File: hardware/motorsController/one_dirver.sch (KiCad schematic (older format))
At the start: 9 parts, among them U1 VNH5019A-E

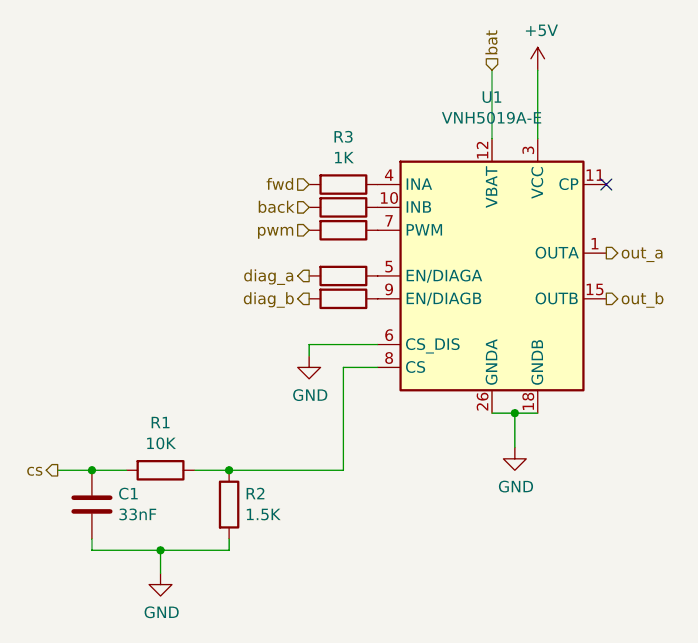
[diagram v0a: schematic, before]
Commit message: layout and connect power for a pair of drivers
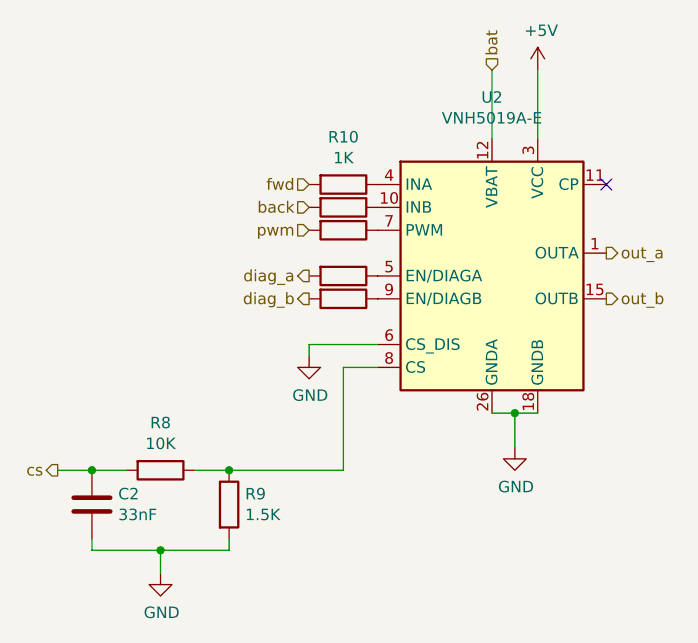
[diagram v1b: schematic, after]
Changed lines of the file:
@@
 $Descr A4 11693 8268
 encoding utf-8
-Sheet 2 5
+Sheet 3 5
 Title ""
 Date ""
@@
 AR Path="/5F8B7961/5F75DD74" Ref="U3"  Part="1"
 AR Path="/5F8B7981/5F75DD74" Ref="U4"  Part="1"
-F 0 "U1" H 3150 3531 50  0000 C CNN
+F 0 "U2" H 3150 3531 50  0000 C CNN
 F 1 "VNH5019A-E" H 3150 3440 50  0000 C CNN
 F 2 "Package_SO:ST_MultiPowerSO-30" H 4050 2200 50  0001 C CNN
@@
 AR Path="/5F8B7961/5F764A13" Ref="R17"  Part="1"
 AR Path="/5F8B7981/5F764A13" Ref="R24"  Part="1"
-F 0 "R3" V 2293 2350 50  0000 C CNN
+F 0 "R10" V 2293 2350 50  0000 C CNN
 F 1 "1K" V 2384 2350 50  0000 C CNN
 F 2 "Resistor_SMD:R_0805_2012Metric" V 2430 2350 50  0001 C CNN
@@
 AR Path="/5F8B7961/5F765406" Ref="R18"  Part="1"
 AR Path="/5F8B7981/5F765406" Ref="R25"  Part="1"
-F 0 "R4" V 2293 2450 50  0001 C CNN
+F 0 "R11" V 2293 2450 50  0001 C CNN
 F 1 "1K" V 2384 2450 50  0001 C CNN
 F 2 "Resistor_SMD:R_0805_2012Metric" V 2430 2450 50  0001 C CNN
@@
 AR Path="/5F8B7961/5F7658F2" Ref="R19"  Part="1"
 AR Path="/5F8B7981/5F7658F2" Ref="R26"  Part="1"
-F 0 "R5" V 2293 2550 50  0001 C CNN
+F 0 "R12" V 2293 2550 50  0001 C CNN
 F 1 "1K" V 2384 2550 50  0001 C CNN
 F 2 "Resistor_SMD:R_0805_2012Metric" V 2430 2550 50  0001 C CNN
@@
 AR Path="/5F8B7961/5F77E0ED" Ref="R20"  Part="1"
 AR Path="/5F8B7981/5F77E0ED" Ref="R27"  Part="1"
-F 0 "R6" V 2293 2750 50  0001 C CNN
+F 0 "R13" V 2293 2750 50  0001 C CNN
 F 1 "1K" V 2384 2750 50  0001 C CNN
 F 2 "Resistor_SMD:R_0805_2012Metric" V 2430 2750 50  0001 C CNN
@@
 AR Path="/5F8B7961/5F781639" Ref="R21"  Part="1"
 AR Path="/5F8B7981/5F781639" Ref="R28"  Part="1"
-F 0 "R7" V 2293 2850 50  0001 C CNN
+F 0 "R14" V 2293 2850 50  0001 C CNN
 F 1 "1K" V 2384 2850 50  0001 C CNN
 F 2 "Resistor_SMD:R_0805_2012Metric" V 2430 2850 50  0001 C CNN
@@
 AR Path="/5F8B7961/5F781B76" Ref="#PWR0112"  Part="1"
 AR Path="/5F8B7981/5F781B76" Ref="#PWR0116"  Part="1"
-F 0 "#PWR0101" H 2350 2850 50  0001 C CNN
+F 0 "#PWR0108" H 2350 2850 50  0001 C CNN
 F 1 "GND" H 2355 2927 50  0000 C CNN
 F 2 "" H 2350 3100 50  0001 C CNN
@@
 AR Path="/5F8B7961/5F782890" Ref="R16"  Part="1"
 AR Path="/5F8B7981/5F782890" Ref="R23"  Part="1"
-F 0 "R2" H 2070 3796 50  0000 L CNN
+F 0 "R9" H 2070 3796 50  0000 L CNN
 F 1 "1.5K" H 2070 3705 50  0000 L CNN
 F 2 "Resistor_SMD:R_0805_2012Metric" V 1930 3750 50  0001 C CNN
@@
 AR Path="/5F8B7961/5F783B44" Ref="#PWR0113"  Part="1"
 AR Path="/5F8B7981/5F783B44" Ref="#PWR0117"  Part="1"
-F 0 "#PWR0102" H 1700 3800 50  0001 C CNN
+F 0 "#PWR0109" H 1700 3800 50  0001 C CNN
 F 1 "GND" H 1705 3877 50  0000 C CNN
 F 2 "" H 1700 4050 50  0001 C CNN
@@
 AR Path="/5F8B7961/5F7841BA" Ref="R15"  Part="1"
 AR Path="/5F8B7981/5F7841BA" Ref="R22"  Part="1"
-F 0 "R1" V 1493 3600 50  0000 C CNN
+F 0 "R8" V 1493 3600 50  0000 C CNN
 F 1 "10K" V 1584 3600 50  0000 C CNN
 F 2 "Resistor_SMD:R_0805_2012Metric" V 1630 3600 50  0001 C CNN
@@
 AR Path="/5F8B7961/5F784D90" Ref="C3"  Part="1"
 AR Path="/5F8B7981/5F784D90" Ref="C4"  Part="1"
-F 0 "C1" H 1515 3796 50  0000 L CNN
+F 0 "C2" H 1515 3796 50  0000 L CNN
 F 1 "33nF" H 1515 3705 50  0000 L CNN
 F 2 "Capacitor_SMD:C_1206_3216Metric" H 1438 3600 50  0001 C CNN
@@
 AR Path="/5F8B7961/5F78A1BC" Ref="#PWR0114"  Part="1"
 AR Path="/5F8B7981/5F78A1BC" Ref="#PWR0118"  Part="1"
-F 0 "#PWR0103" H 3350 1700 50  0001 C CNN
+F 0 "#PWR0110" H 3350 1700 50  0001 C CNN
 F 1 "+5V" H 3365 2023 50  0000 C CNN
 F 2 "" H 3350 1850 50  0001 C CNN
@@
 AR Path="/5F8B7961/5F794080" Ref="#PWR0115"  Part="1"
 AR Path="/5F8B7981/5F794080" Ref="#PWR0119"  Part="1"
-F 0 "#PWR0104" H 3250 3250 50  0001 C CNN
+F 0 "#PWR0111" H 3250 3250 50  0001 C CNN
 F 1 "GND" H 3255 3327 50  0000 C CNN
 F 2 "" H 3250 3500 50  0001 C CNN

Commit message: connect left-rear driver to arduino
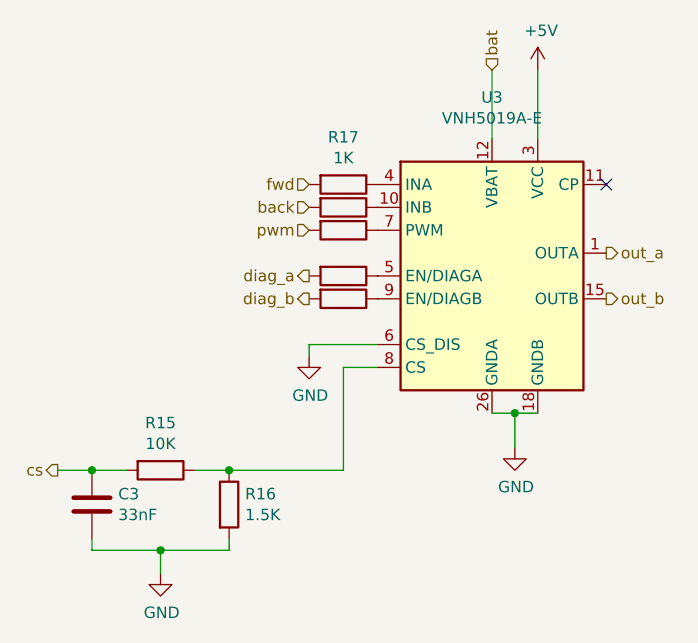
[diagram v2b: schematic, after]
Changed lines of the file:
@@
 $Descr A4 11693 8268
 encoding utf-8
-Sheet 3 5
+Sheet 4 5
 Title ""
 Date ""
@@
 AR Path="/5F8B7961/5F75DD74" Ref="U3"  Part="1"
 AR Path="/5F8B7981/5F75DD74" Ref="U4"  Part="1"
-F 0 "U2" H 3150 3531 50  0000 C CNN
+F 0 "U3" H 3150 3531 50  0000 C CNN
 F 1 "VNH5019A-E" H 3150 3440 50  0000 C CNN
 F 2 "Package_SO:ST_MultiPowerSO-30" H 4050 2200 50  0001 C CNN
@@
 AR Path="/5F8B7961/5F764A13" Ref="R17"  Part="1"
 AR Path="/5F8B7981/5F764A13" Ref="R24"  Part="1"
-F 0 "R10" V 2293 2350 50  0000 C CNN
+F 0 "R17" V 2293 2350 50  0000 C CNN
 F 1 "1K" V 2384 2350 50  0000 C CNN
 F 2 "Resistor_SMD:R_0805_2012Metric" V 2430 2350 50  0001 C CNN
@@
 AR Path="/5F8B7961/5F765406" Ref="R18"  Part="1"
 AR Path="/5F8B7981/5F765406" Ref="R25"  Part="1"
-F 0 "R11" V 2293 2450 50  0001 C CNN
+F 0 "R18" V 2293 2450 50  0001 C CNN
 F 1 "1K" V 2384 2450 50  0001 C CNN
 F 2 "Resistor_SMD:R_0805_2012Metric" V 2430 2450 50  0001 C CNN
@@
 AR Path="/5F8B7961/5F7658F2" Ref="R19"  Part="1"
 AR Path="/5F8B7981/5F7658F2" Ref="R26"  Part="1"
-F 0 "R12" V 2293 2550 50  0001 C CNN
+F 0 "R19" V 2293 2550 50  0001 C CNN
 F 1 "1K" V 2384 2550 50  0001 C CNN
 F 2 "Resistor_SMD:R_0805_2012Metric" V 2430 2550 50  0001 C CNN
@@
 AR Path="/5F8B7961/5F77E0ED" Ref="R20"  Part="1"
 AR Path="/5F8B7981/5F77E0ED" Ref="R27"  Part="1"
-F 0 "R13" V 2293 2750 50  0001 C CNN
+F 0 "R20" V 2293 2750 50  0001 C CNN
 F 1 "1K" V 2384 2750 50  0001 C CNN
 F 2 "Resistor_SMD:R_0805_2012Metric" V 2430 2750 50  0001 C CNN
@@
 AR Path="/5F8B7961/5F781639" Ref="R21"  Part="1"
 AR Path="/5F8B7981/5F781639" Ref="R28"  Part="1"
-F 0 "R14" V 2293 2850 50  0001 C CNN
+F 0 "R21" V 2293 2850 50  0001 C CNN
 F 1 "1K" V 2384 2850 50  0001 C CNN
 F 2 "Resistor_SMD:R_0805_2012Metric" V 2430 2850 50  0001 C CNN
@@
 AR Path="/5F8B7961/5F781B76" Ref="#PWR0112"  Part="1"
 AR Path="/5F8B7981/5F781B76" Ref="#PWR0116"  Part="1"
-F 0 "#PWR0108" H 2350 2850 50  0001 C CNN
+F 0 "#PWR0116" H 2350 2850 50  0001 C CNN
 F 1 "GND" H 2355 2927 50  0000 C CNN
 F 2 "" H 2350 3100 50  0001 C CNN
@@
 AR Path="/5F8B7961/5F782890" Ref="R16"  Part="1"
 AR Path="/5F8B7981/5F782890" Ref="R23"  Part="1"
-F 0 "R9" H 2070 3796 50  0000 L CNN
+F 0 "R16" H 2070 3796 50  0000 L CNN
 F 1 "1.5K" H 2070 3705 50  0000 L CNN
 F 2 "Resistor_SMD:R_0805_2012Metric" V 1930 3750 50  0001 C CNN
@@
 AR Path="/5F8B7961/5F783B44" Ref="#PWR0113"  Part="1"
 AR Path="/5F8B7981/5F783B44" Ref="#PWR0117"  Part="1"
-F 0 "#PWR0109" H 1700 3800 50  0001 C CNN
+F 0 "#PWR0117" H 1700 3800 50  0001 C CNN
 F 1 "GND" H 1705 3877 50  0000 C CNN
 F 2 "" H 1700 4050 50  0001 C CNN
@@
 AR Path="/5F8B7961/5F7841BA" Ref="R15"  Part="1"
 AR Path="/5F8B7981/5F7841BA" Ref="R22"  Part="1"
-F 0 "R8" V 1493 3600 50  0000 C CNN
+F 0 "R15" V 1493 3600 50  0000 C CNN
 F 1 "10K" V 1584 3600 50  0000 C CNN
 F 2 "Resistor_SMD:R_0805_2012Metric" V 1630 3600 50  0001 C CNN
@@
 AR Path="/5F8B7961/5F784D90" Ref="C3"  Part="1"
 AR Path="/5F8B7981/5F784D90" Ref="C4"  Part="1"
-F 0 "C2" H 1515 3796 50  0000 L CNN
+F 0 "C3" H 1515 3796 50  0000 L CNN
 F 1 "33nF" H 1515 3705 50  0000 L CNN
 F 2 "Capacitor_SMD:C_1206_3216Metric" H 1438 3600 50  0001 C CNN
@@
 AR Path="/5F8B7961/5F78A1BC" Ref="#PWR0114"  Part="1"
 AR Path="/5F8B7981/5F78A1BC" Ref="#PWR0118"  Part="1"
-F 0 "#PWR0110" H 3350 1700 50  0001 C CNN
+F 0 "#PWR0118" H 3350 1700 50  0001 C CNN
 F 1 "+5V" H 3365 2023 50  0000 C CNN
 F 2 "" H 3350 1850 50  0001 C CNN
@@
 AR Path="/5F8B7961/5F794080" Ref="#PWR0115"  Part="1"
 AR Path="/5F8B7981/5F794080" Ref="#PWR0119"  Part="1"
-F 0 "#PWR0111" H 3250 3250 50  0001 C CNN
+F 0 "#PWR0119" H 3250 3250 50  0001 C CNN
 F 1 "GND" H 3255 3327 50  0000 C CNN
 F 2 "" H 3250 3500 50  0001 C CNN

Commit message: reconnect right-rear driver to more conenient pins
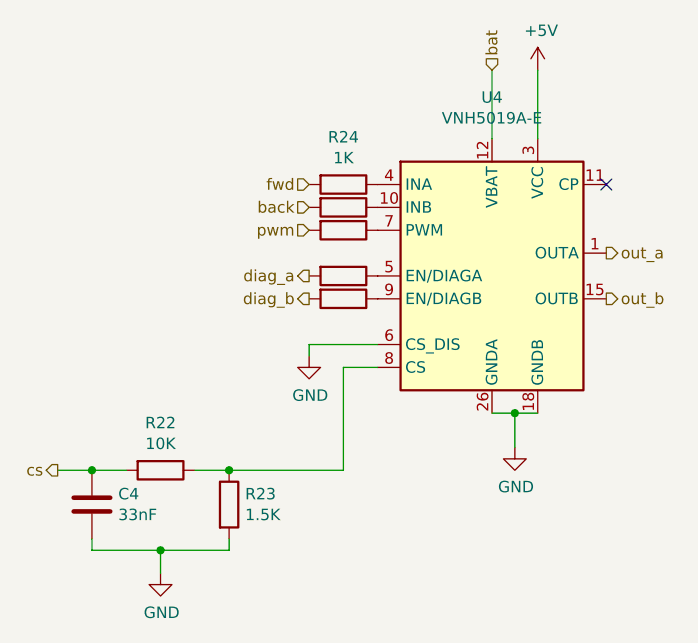
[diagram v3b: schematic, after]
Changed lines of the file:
@@
 $Descr A4 11693 8268
 encoding utf-8
-Sheet 4 5
+Sheet 5 5
 Title ""
 Date ""
@@
 AR Path="/5F8B7961/5F75DD74" Ref="U3"  Part="1"
 AR Path="/5F8B7981/5F75DD74" Ref="U4"  Part="1"
-F 0 "U3" H 3150 3531 50  0000 C CNN
+F 0 "U4" H 3150 3531 50  0000 C CNN
 F 1 "VNH5019A-E" H 3150 3440 50  0000 C CNN
 F 2 "Package_SO:ST_MultiPowerSO-30" H 4050 2200 50  0001 C CNN
@@
 AR Path="/5F8B7961/5F764A13" Ref="R17"  Part="1"
 AR Path="/5F8B7981/5F764A13" Ref="R24"  Part="1"
-F 0 "R17" V 2293 2350 50  0000 C CNN
+F 0 "R24" V 2293 2350 50  0000 C CNN
 F 1 "1K" V 2384 2350 50  0000 C CNN
 F 2 "Resistor_SMD:R_0805_2012Metric" V 2430 2350 50  0001 C CNN
@@
 AR Path="/5F8B7961/5F765406" Ref="R18"  Part="1"
 AR Path="/5F8B7981/5F765406" Ref="R25"  Part="1"
-F 0 "R18" V 2293 2450 50  0001 C CNN
+F 0 "R25" V 2293 2450 50  0001 C CNN
 F 1 "1K" V 2384 2450 50  0001 C CNN
 F 2 "Resistor_SMD:R_0805_2012Metric" V 2430 2450 50  0001 C CNN
@@
 AR Path="/5F8B7961/5F7658F2" Ref="R19"  Part="1"
 AR Path="/5F8B7981/5F7658F2" Ref="R26"  Part="1"
-F 0 "R19" V 2293 2550 50  0001 C CNN
+F 0 "R26" V 2293 2550 50  0001 C CNN
 F 1 "1K" V 2384 2550 50  0001 C CNN
 F 2 "Resistor_SMD:R_0805_2012Metric" V 2430 2550 50  0001 C CNN
@@
 AR Path="/5F8B7961/5F77E0ED" Ref="R20"  Part="1"
 AR Path="/5F8B7981/5F77E0ED" Ref="R27"  Part="1"
-F 0 "R20" V 2293 2750 50  0001 C CNN
+F 0 "R27" V 2293 2750 50  0001 C CNN
 F 1 "1K" V 2384 2750 50  0001 C CNN
 F 2 "Resistor_SMD:R_0805_2012Metric" V 2430 2750 50  0001 C CNN
@@
 AR Path="/5F8B7961/5F781639" Ref="R21"  Part="1"
 AR Path="/5F8B7981/5F781639" Ref="R28"  Part="1"
-F 0 "R21" V 2293 2850 50  0001 C CNN
+F 0 "R28" V 2293 2850 50  0001 C CNN
 F 1 "1K" V 2384 2850 50  0001 C CNN
 F 2 "Resistor_SMD:R_0805_2012Metric" V 2430 2850 50  0001 C CNN
@@
 AR Path="/5F8B7961/5F782890" Ref="R16"  Part="1"
 AR Path="/5F8B7981/5F782890" Ref="R23"  Part="1"
-F 0 "R16" H 2070 3796 50  0000 L CNN
+F 0 "R23" H 2070 3796 50  0000 L CNN
 F 1 "1.5K" H 2070 3705 50  0000 L CNN
 F 2 "Resistor_SMD:R_0805_2012Metric" V 1930 3750 50  0001 C CNN
@@
 AR Path="/5F8B7961/5F7841BA" Ref="R15"  Part="1"
 AR Path="/5F8B7981/5F7841BA" Ref="R22"  Part="1"
-F 0 "R15" V 1493 3600 50  0000 C CNN
+F 0 "R22" V 1493 3600 50  0000 C CNN
 F 1 "10K" V 1584 3600 50  0000 C CNN
 F 2 "Resistor_SMD:R_0805_2012Metric" V 1630 3600 50  0001 C CNN
@@
 AR Path="/5F8B7961/5F784D90" Ref="C3"  Part="1"
 AR Path="/5F8B7981/5F784D90" Ref="C4"  Part="1"
-F 0 "C3" H 1515 3796 50  0000 L CNN
+F 0 "C4" H 1515 3796 50  0000 L CNN
 F 1 "33nF" H 1515 3705 50  0000 L CNN
 F 2 "Capacitor_SMD:C_1206_3216Metric" H 1438 3600 50  0001 C CNN

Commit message: connect left-front driver to arduino
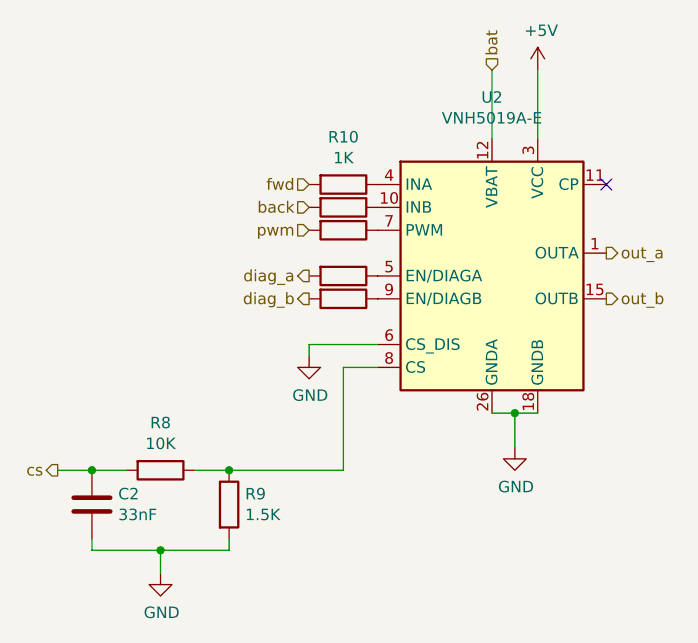
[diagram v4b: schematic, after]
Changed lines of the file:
@@
 $Descr A4 11693 8268
 encoding utf-8
-Sheet 5 5
+Sheet 3 5
 Title ""
 Date ""
@@
 AR Path="/5F8B7961/5F75DD74" Ref="U3"  Part="1"
 AR Path="/5F8B7981/5F75DD74" Ref="U4"  Part="1"
-F 0 "U4" H 3150 3531 50  0000 C CNN
+F 0 "U2" H 3150 3531 50  0000 C CNN
 F 1 "VNH5019A-E" H 3150 3440 50  0000 C CNN
 F 2 "Package_SO:ST_MultiPowerSO-30" H 4050 2200 50  0001 C CNN
@@
 AR Path="/5F8B7961/5F764A13" Ref="R17"  Part="1"
 AR Path="/5F8B7981/5F764A13" Ref="R24"  Part="1"
-F 0 "R24" V 2293 2350 50  0000 C CNN
+F 0 "R10" V 2293 2350 50  0000 C CNN
 F 1 "1K" V 2384 2350 50  0000 C CNN
 F 2 "Resistor_SMD:R_0805_2012Metric" V 2430 2350 50  0001 C CNN
@@
 AR Path="/5F8B7961/5F765406" Ref="R18"  Part="1"
 AR Path="/5F8B7981/5F765406" Ref="R25"  Part="1"
-F 0 "R25" V 2293 2450 50  0001 C CNN
+F 0 "R11" V 2293 2450 50  0001 C CNN
 F 1 "1K" V 2384 2450 50  0001 C CNN
 F 2 "Resistor_SMD:R_0805_2012Metric" V 2430 2450 50  0001 C CNN
@@
 AR Path="/5F8B7961/5F7658F2" Ref="R19"  Part="1"
 AR Path="/5F8B7981/5F7658F2" Ref="R26"  Part="1"
-F 0 "R26" V 2293 2550 50  0001 C CNN
+F 0 "R12" V 2293 2550 50  0001 C CNN
 F 1 "1K" V 2384 2550 50  0001 C CNN
 F 2 "Resistor_SMD:R_0805_2012Metric" V 2430 2550 50  0001 C CNN
@@
 AR Path="/5F8B7961/5F77E0ED" Ref="R20"  Part="1"
 AR Path="/5F8B7981/5F77E0ED" Ref="R27"  Part="1"
-F 0 "R27" V 2293 2750 50  0001 C CNN
+F 0 "R13" V 2293 2750 50  0001 C CNN
 F 1 "1K" V 2384 2750 50  0001 C CNN
 F 2 "Resistor_SMD:R_0805_2012Metric" V 2430 2750 50  0001 C CNN
@@
 AR Path="/5F8B7961/5F781639" Ref="R21"  Part="1"
 AR Path="/5F8B7981/5F781639" Ref="R28"  Part="1"
-F 0 "R28" V 2293 2850 50  0001 C CNN
+F 0 "R14" V 2293 2850 50  0001 C CNN
 F 1 "1K" V 2384 2850 50  0001 C CNN
 F 2 "Resistor_SMD:R_0805_2012Metric" V 2430 2850 50  0001 C CNN
@@
 AR Path="/5F8B7961/5F782890" Ref="R16"  Part="1"
 AR Path="/5F8B7981/5F782890" Ref="R23"  Part="1"
-F 0 "R23" H 2070 3796 50  0000 L CNN
+F 0 "R9" H 2070 3796 50  0000 L CNN
 F 1 "1.5K" H 2070 3705 50  0000 L CNN
 F 2 "Resistor_SMD:R_0805_2012Metric" V 1930 3750 50  0001 C CNN
@@
 AR Path="/5F8B7961/5F7841BA" Ref="R15"  Part="1"
 AR Path="/5F8B7981/5F7841BA" Ref="R22"  Part="1"
-F 0 "R22" V 1493 3600 50  0000 C CNN
+F 0 "R8" V 1493 3600 50  0000 C CNN
 F 1 "10K" V 1584 3600 50  0000 C CNN
 F 2 "Resistor_SMD:R_0805_2012Metric" V 1630 3600 50  0001 C CNN
@@
 AR Path="/5F8B7961/5F784D90" Ref="C3"  Part="1"
 AR Path="/5F8B7981/5F784D90" Ref="C4"  Part="1"
-F 0 "C4" H 1515 3796 50  0000 L CNN
+F 0 "C2" H 1515 3796 50  0000 L CNN
 F 1 "33nF" H 1515 3705 50  0000 L CNN
 F 2 "Capacitor_SMD:C_1206_3216Metric" H 1438 3600 50  0001 C CNN

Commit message: add an i2c connector
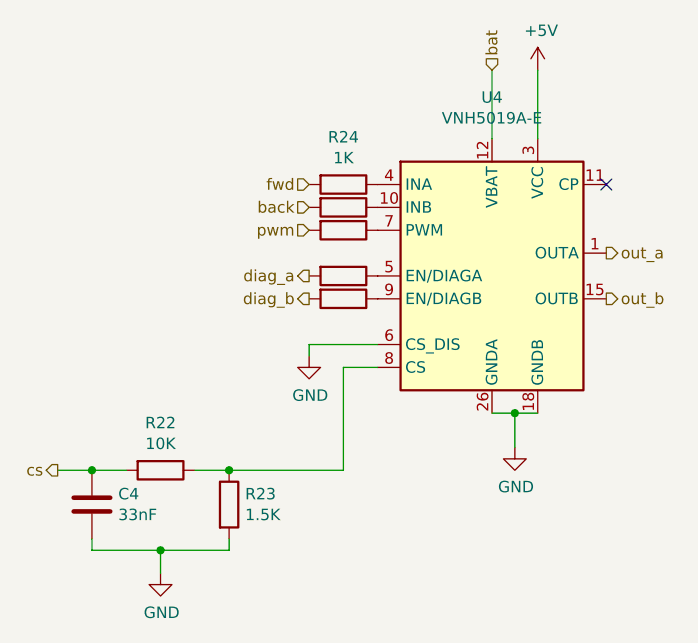
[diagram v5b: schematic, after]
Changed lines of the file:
@@
 AR Path="/5F8B7961/5F75DD74" Ref="U3"  Part="1"
 AR Path="/5F8B7981/5F75DD74" Ref="U4"  Part="1"
-F 0 "U2" H 3150 3531 50  0000 C CNN
+F 0 "U4" H 3150 3531 50  0000 C CNN
 F 1 "VNH5019A-E" H 3150 3440 50  0000 C CNN
 F 2 "Package_SO:ST_MultiPowerSO-30" H 4050 2200 50  0001 C CNN
@@
 AR Path="/5F8B7961/5F764A13" Ref="R17"  Part="1"
 AR Path="/5F8B7981/5F764A13" Ref="R24"  Part="1"
-F 0 "R10" V 2293 2350 50  0000 C CNN
+F 0 "R24" V 2293 2350 50  0000 C CNN
 F 1 "1K" V 2384 2350 50  0000 C CNN
 F 2 "Resistor_SMD:R_0805_2012Metric" V 2430 2350 50  0001 C CNN
@@
 AR Path="/5F8B7961/5F765406" Ref="R18"  Part="1"
 AR Path="/5F8B7981/5F765406" Ref="R25"  Part="1"
-F 0 "R11" V 2293 2450 50  0001 C CNN
+F 0 "R25" V 2293 2450 50  0001 C CNN
 F 1 "1K" V 2384 2450 50  0001 C CNN
 F 2 "Resistor_SMD:R_0805_2012Metric" V 2430 2450 50  0001 C CNN
@@
 AR Path="/5F8B7961/5F7658F2" Ref="R19"  Part="1"
 AR Path="/5F8B7981/5F7658F2" Ref="R26"  Part="1"
-F 0 "R12" V 2293 2550 50  0001 C CNN
+F 0 "R26" V 2293 2550 50  0001 C CNN
 F 1 "1K" V 2384 2550 50  0001 C CNN
 F 2 "Resistor_SMD:R_0805_2012Metric" V 2430 2550 50  0001 C CNN
@@
 AR Path="/5F8B7961/5F77E0ED" Ref="R20"  Part="1"
 AR Path="/5F8B7981/5F77E0ED" Ref="R27"  Part="1"
-F 0 "R13" V 2293 2750 50  0001 C CNN
+F 0 "R27" V 2293 2750 50  0001 C CNN
 F 1 "1K" V 2384 2750 50  0001 C CNN
 F 2 "Resistor_SMD:R_0805_2012Metric" V 2430 2750 50  0001 C CNN
@@
 AR Path="/5F8B7961/5F781639" Ref="R21"  Part="1"
 AR Path="/5F8B7981/5F781639" Ref="R28"  Part="1"
-F 0 "R14" V 2293 2850 50  0001 C CNN
+F 0 "R28" V 2293 2850 50  0001 C CNN
 F 1 "1K" V 2384 2850 50  0001 C CNN
 F 2 "Resistor_SMD:R_0805_2012Metric" V 2430 2850 50  0001 C CNN
@@
 AR Path="/5F8B7961/5F782890" Ref="R16"  Part="1"
 AR Path="/5F8B7981/5F782890" Ref="R23"  Part="1"
-F 0 "R9" H 2070 3796 50  0000 L CNN
+F 0 "R23" H 2070 3796 50  0000 L CNN
 F 1 "1.5K" H 2070 3705 50  0000 L CNN
 F 2 "Resistor_SMD:R_0805_2012Metric" V 1930 3750 50  0001 C CNN
@@
 AR Path="/5F8B7961/5F7841BA" Ref="R15"  Part="1"
 AR Path="/5F8B7981/5F7841BA" Ref="R22"  Part="1"
-F 0 "R8" V 1493 3600 50  0000 C CNN
+F 0 "R22" V 1493 3600 50  0000 C CNN
 F 1 "10K" V 1584 3600 50  0000 C CNN
 F 2 "Resistor_SMD:R_0805_2012Metric" V 1630 3600 50  0001 C CNN
@@
 AR Path="/5F8B7961/5F784D90" Ref="C3"  Part="1"
 AR Path="/5F8B7981/5F784D90" Ref="C4"  Part="1"
-F 0 "C2" H 1515 3796 50  0000 L CNN
+F 0 "C4" H 1515 3796 50  0000 L CNN
 F 1 "33nF" H 1515 3705 50  0000 L CNN
 F 2 "Capacitor_SMD:C_1206_3216Metric" H 1438 3600 50  0001 C CNN
